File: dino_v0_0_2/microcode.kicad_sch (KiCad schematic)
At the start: 10 parts, among them U15 AT28C64B, U16 74LS244N, U17 74LS244N, U23 AT28C64B, U9 AT28C64B

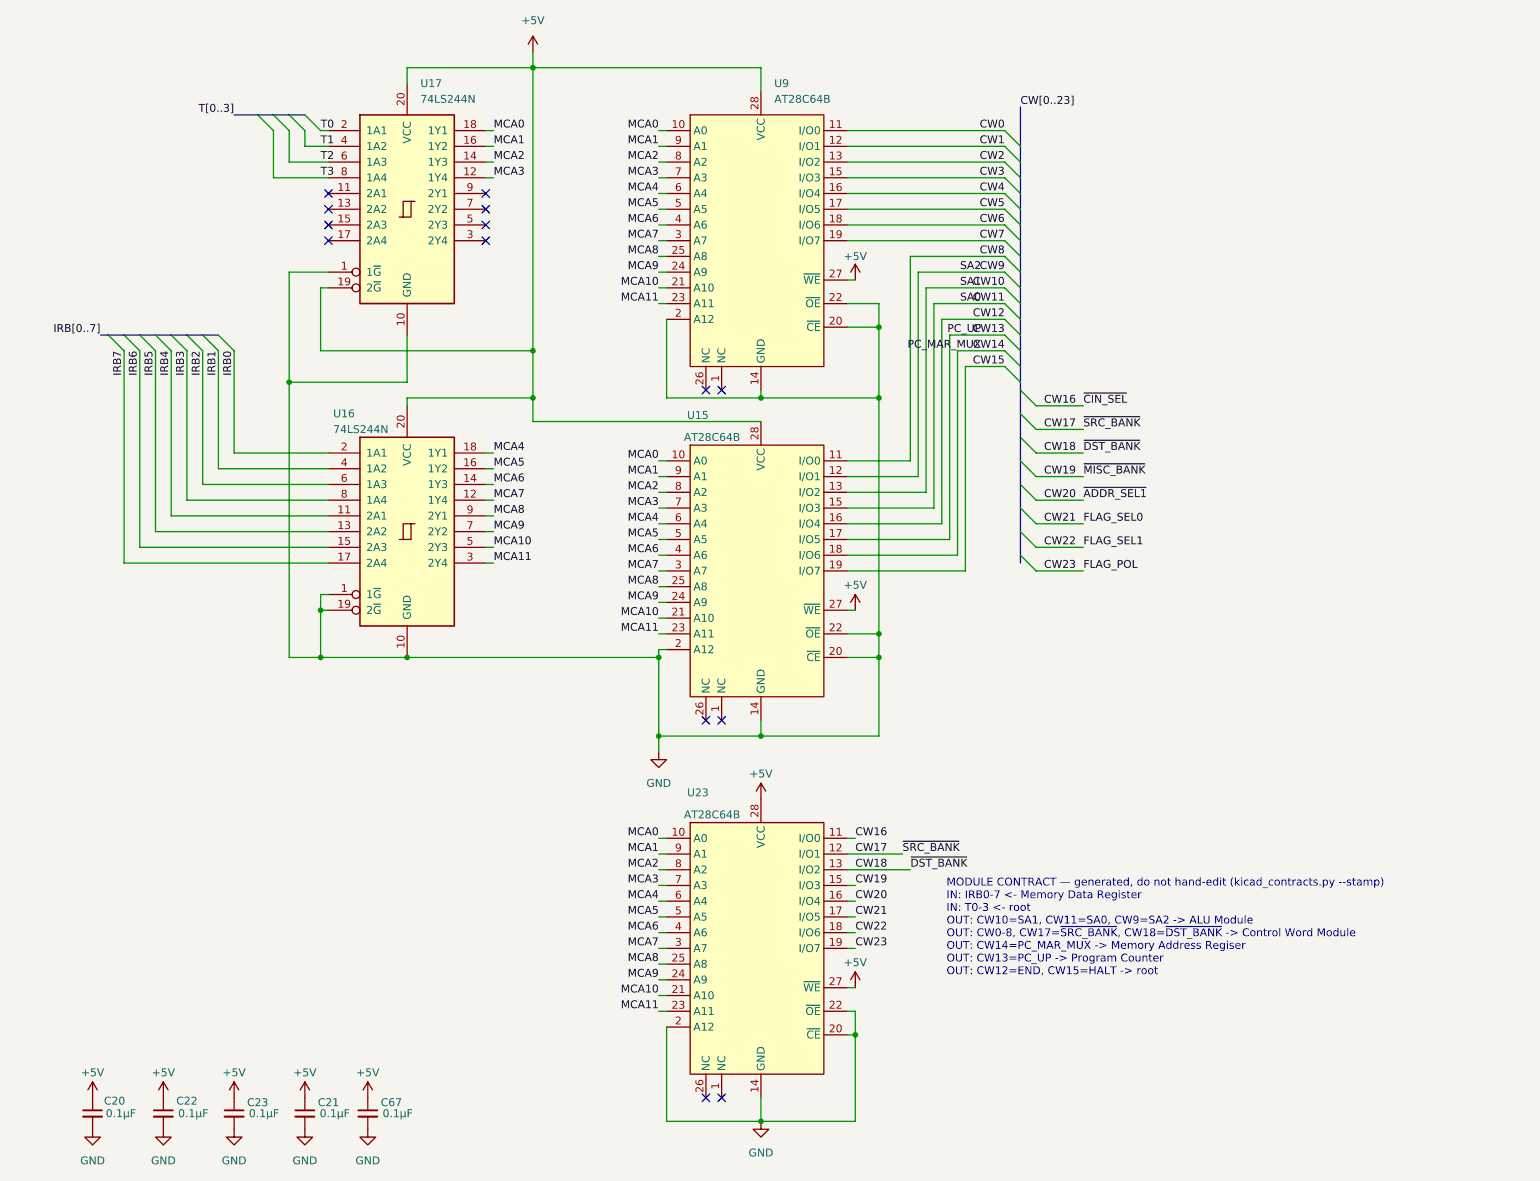
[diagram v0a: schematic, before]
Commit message: feat(kicad): footprints, power sheet, global labels, PCB draft
Every symbol gets a stock THT footprint (plain DIP, no sockets, so the
3D render shows ICs). New Power sheet: 24-pin ATX header for a picoPSU,
rails +5V/+3.3V/+12V/-12V/GND only; no -5V exists on any ATX unit since
2003, none drawn. PS_ON# on a 2-pin header.

Cross-sheet labels become global labels. KiCad joined nothing between
sheets before: 122 base names were split per sheet, ERC saw 90 undriven
inputs whose driver sat one sheet away, and the PCB ratsnest stopped at
every sheet boundary. Proof: KiCad's netlist after equals a name-join of
its netlist before plus the 15 CW alias pairs, pin for pin.

kicad_contracts took a node's sheet from the net name's /Sheet/ prefix;
global nets have none, so it emitted an empty contracts doc. Sheet now
comes from the component's own path; the doc regenerates with zero diff.

ERC 477 -> 2. Real fixes: ROM I/O pins input -> tri_state, '382 GND pin
power_out -> power_in, four orphan symbols rehomed to project lib `dino`,
one stub wire. 133 by-design warnings excluded by uuid ('245 readback on
counter Q, alias stubs, probe-point labels); the two left are bus
signals the peripheral bus sheet will consume.

PCB draft: 198 footprints placed per sheet, all pads netted, no tracks.

Co-Authored-By: Claude Fable 5.1 <noreply@anthropic.com>
Claude-Session: https://claude.ai/code/session_018irreFHb1xEykW5kCD26ow
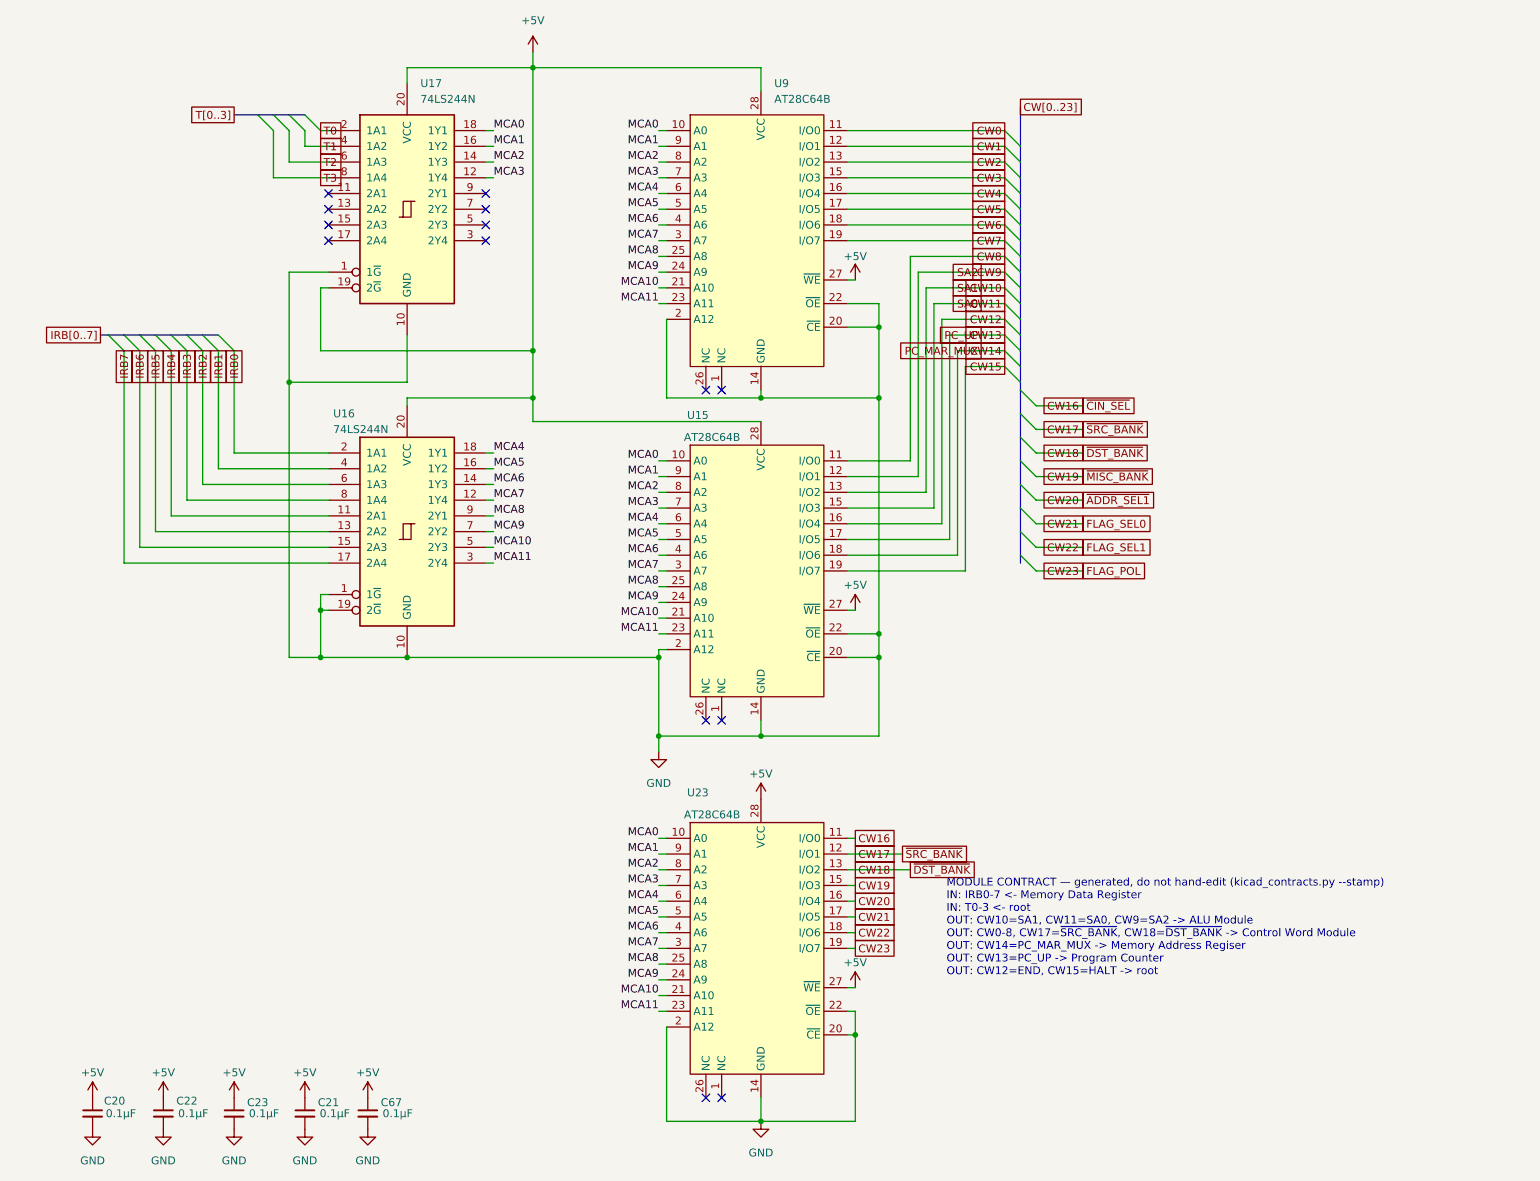
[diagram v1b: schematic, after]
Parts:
- C20, C21, C22, C23, C67: footprint (none) -> Capacitor_THT:C_Disc_D5.0mm_W2.5mm_P2.50mm
- U15, U23, U9: footprint (none) -> Package_DIP:DIP-28_W15.24mm; symbol Memory_EEPROM:AT28C64B -> dino:AT28C64B
- U16, U17: footprint (none) -> Package_DIP:DIP-20_W7.62mm; symbol 74xx:74LS244N -> dino:74LS244N

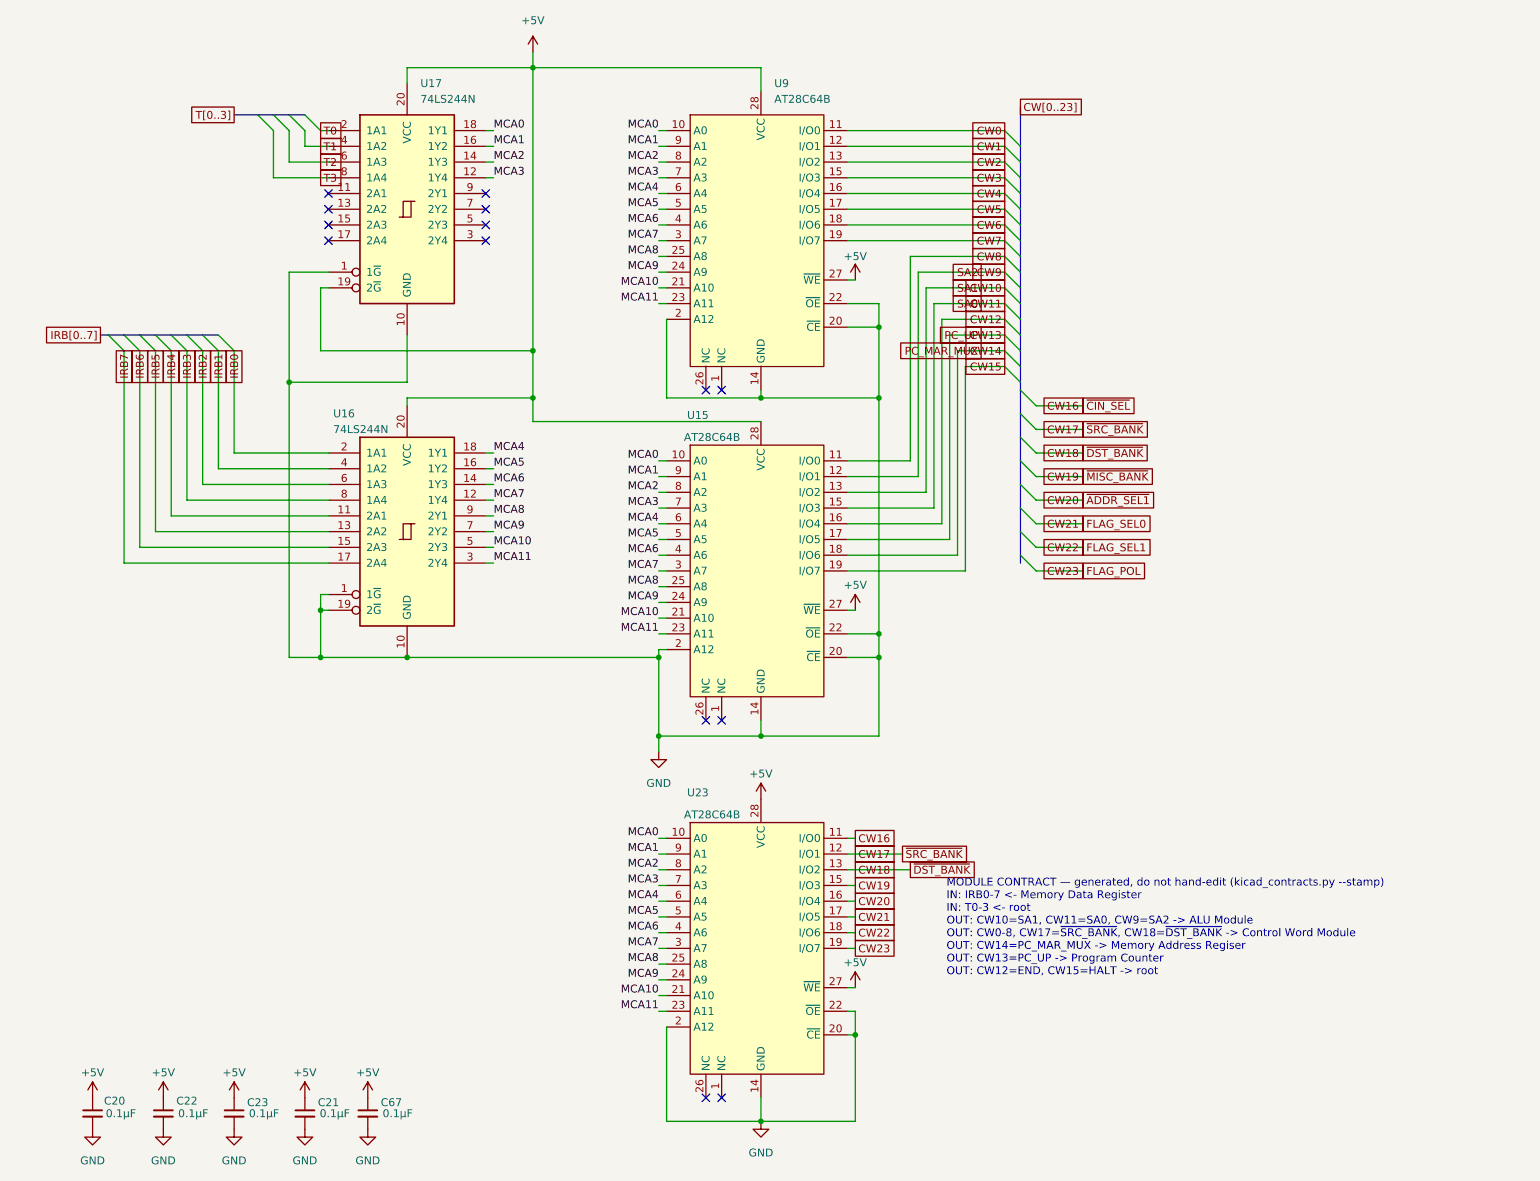
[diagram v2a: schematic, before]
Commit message: feat(int): draw the interrupt block; sheet cleanup pass
New sheet dino_v0_0_2/interrupt.kicad_sch (page 15): U80-U87, R28 4.7k
pull-up on ~{IRQ}, R29 100R on the block's CLK branch, C83-C90. Every
pin per PHASE_INT SECTION 3, checked against the plan with kicad_netlist
and kicad-cli (146 pins, 0 mismatches).

Old sheets (SECTION 3.2): U28.4 lifted off GND to INJECT; U61.3 to
END_OR_ACCEPT; U36.1 to PC_UP_GATED; U49 D0-3 cut from U48 Za-Zd and
routed through U87 as FLAG_NEXT0-3 / FLAG_D0-3; FLAG_C/Z/V/N and the
five decoder outputs made global. dino_serial: U104 74LS05, INTR ->
~{IRQ}, C4.

Placement pass on every sheet: bus entries and global labels no longer
share wires; M, CW, T, IRB and SA buses kept as labelled keys. Nets
diffed against HEAD per sheet: only the intended changes and a rotated
C29. Project ERC: 0 errors. MODULE CONTRACT stamps regenerated.

Co-Authored-By: Claude Fable 5.1 <noreply@anthropic.com>
Claude-Session: https://claude.ai/code/session_01JGxSS4MVUcaZdKZGtKroSg
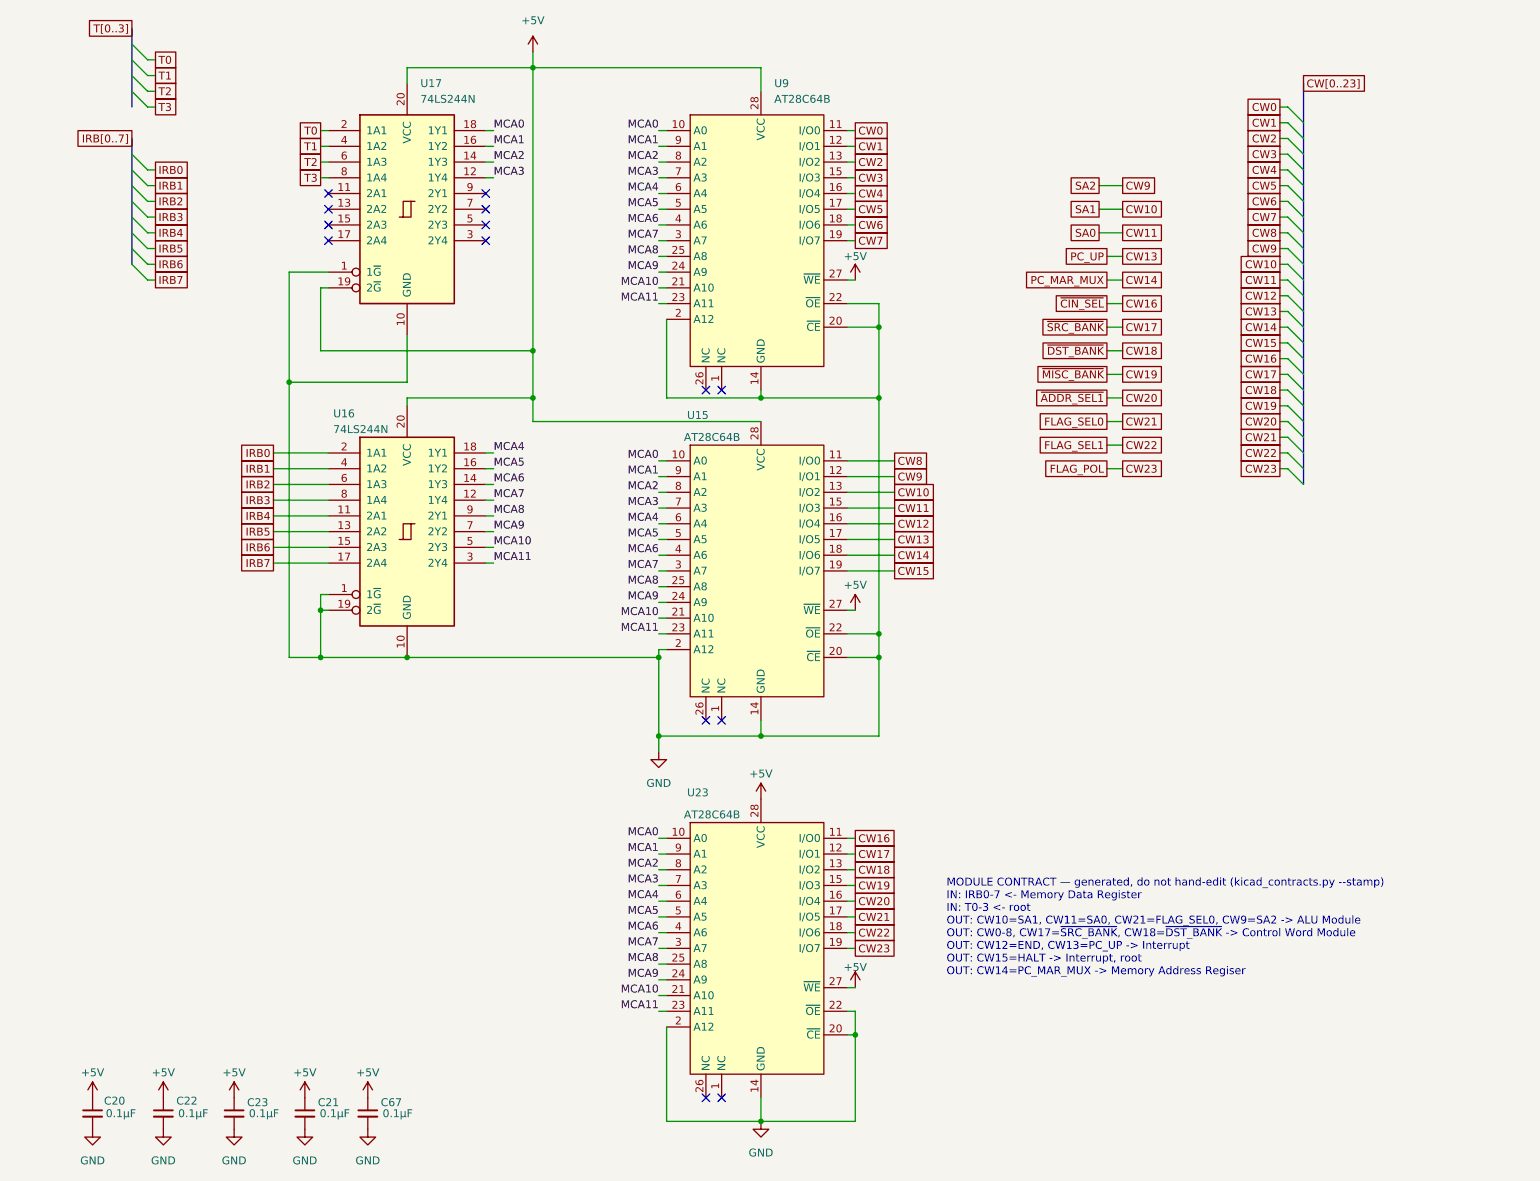
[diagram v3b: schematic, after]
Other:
- note added: "MODULE CONTRACT — generated, do not hand-edit (kicad_contracts.py --stamp) IN: IRB0-7 <- Memory Data Register IN: T0-3 <- root OUT: CW10=SA1, CW11=SA0, CW21=FLAG_SEL0, CW9=SA2 -> ALU Module OUT: CW0-8, CW17=~{SRC_BANK}, CW18=~{DST_BANK} -> Control Word Module OUT: CW12=END, CW13=PC_UP -> Interrupt OUT: CW15=HALT -> Interrupt, root OUT: CW14=PC_MAR_MUX -> Memory Address Regiser"
- note removed: "MODULE CONTRACT — generated, do not hand-edit (kicad_contracts.py --stamp) IN: IRB0-7 <- Memory Data Register IN: T0-3 <- root OUT: CW10=SA1, CW11=SA0, CW9=SA2 -> ALU Module OUT: CW0-8, CW17=~{SRC_BANK}, CW18=~{DST_BANK} -> Control Word Module OUT: CW14=PC_MAR_MUX -> Memory Address Regiser OUT: CW13=PC_UP -> Program Counter OUT: CW12=END, CW15=HALT -> root"
